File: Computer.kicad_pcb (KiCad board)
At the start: 2 copper layers, 35 parts, among them J1 DB9, J2 Screw_Terminal_1x04, U1 8284, U10 74LS04, U11 7400, U12 8259, U2 LM2931AZ-5.0, U3 8088, U4 74LS04, U5 28C256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

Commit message: Fix GND fill issue
There was an area of the copper fill on B.Cu that wasn't getting any
connection to ground. I fixed this here.
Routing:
- net Net-(U4-Pad10): track 130.2 -> 131.0 mm, vias 2 -> 4
- net Net-(U4-Pad11): track 167.5 -> 168.3 mm, vias 2 -> 4

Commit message: Update to revision A
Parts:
- added R16: 10k, Resistors_THT:R_Axial_DIN0204_L3.6mm_D1.6mm_P7.62mm_Horizontal, F.Cu at (163.8, 57.1)
- added R17: 10k, Resistors_THT:R_Axial_DIN0204_L3.6mm_D1.6mm_P7.62mm_Horizontal, F.Cu at (147.3, 55.9)
- added R4: 10k, Resistors_THT:R_Axial_DIN0204_L3.6mm_D1.6mm_P7.62mm_Horizontal, F.Cu at (139.7, 119.4)
- added R5: 10k, Resistors_THT:R_Axial_DIN0204_L3.6mm_D1.6mm_P7.62mm_Horizontal, F.Cu at (123.2, 134.6)
- added U13: 74LS138, Housings_DIP:DIP-16_W7.62mm, F.Cu at (152.4, 39.4)
- U8: value 7400 -> 74LS138; footprint Housings_DIP:DIP-14_W7.62mm -> Housings_DIP:DIP-16_W7.62mm
- moved R11 60.4 mm to (97.8, 71.1), turned to 90 degrees
- moved C2 57.5 mm to (159.1, 74.9), turned to 0 degrees
- moved U11 47.8 mm to (135.9, 41.9)
- moved U8 47.7 mm to (127.0, 119.4), turned to 0 degrees
- moved R2 47.1 mm to (158.8, 63.5), turned to 270 degrees
- moved R3 45.4 mm to (158.8, 91.4), turned to 270 degrees
- moved BUS1 43.2 mm to (172.7, 123.2)
- moved R1 42.4 mm to (129.5, 48.3), turned to 270 degrees
- moved C4 42.2 mm to (58.4, 109.2)
- moved U5 40.2 mm to (102.9, 63.5)
- moved R8 39.1 mm to (134.6, 78.7), turned to 270 degrees
- moved C1 38.7 mm to (54.6, 48.3), turned to 180 degrees
- moved R10 38.6 mm to (134.6, 90.2), turned to 270 degrees
- moved R12 38.1 mm to (68.6, 113.0)
- moved U7 38.1 mm to (72.4, 63.5)
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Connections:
- U10 pad 10: (no net) -> Net-(U10-Pad10)
- U10 pad 11: (no net) -> WR
- U10 pad 12: (no net) -> Net-(U10-Pad12)
- U10 pad 13: (no net) -> IO/M
- U10 pad 3: IO/M -> RD
- U10 pad 5: IO/M -> RD
- U10 pad 9: IO/M -> RD
- U12 pad 1: Net-(U10-Pad8) -> Net-(U12-Pad1)
- U12 pad 2: Net-(U10-Pad8) -> RD
- U12 pad 3: Net-(U10-Pad8) -> Net-(U10-Pad10)
- U3 pad 32: IO/M -> RD
- U4 pad 10: Net-(U4-Pad10) -> (no net)
- U4 pad 11: Net-(U4-Pad11) -> (no net)
- U4 pad 3: Net-(U4-Pad3) -> (no net)
- U4 pad 4: IO/M -> (no net)
- U4 pad 5: Net-(U4-Pad2) -> (no net)
- U4 pad 6: Net-(U4-Pad3) -> (no net)
- U4 pad 8: Net-(U4-Pad8) -> (no net)
- U4 pad 9: IO/M -> (no net)
- U5 pad 20: Net-(U4-Pad10) -> Net-(U5-Pad20)
- U5 pad 22: IO/M -> RD
- U5 pad 27: Net-(U4-Pad10) -> Net-(R11-Pad1)
- U6 pad 20: Net-(U4-Pad11) -> Net-(U6-Pad20)
- U6 pad 22: IO/M -> RD
- U7 pad 14: Net-(U4-Pad8) -> Net-(U13-Pad15)
- U7 pad 21: IO/M -> Net-(U10-Pad8)
- U8 pad 1: A15 -> A17
- U8 pad 10: Net-(R11-Pad1) -> Net-(U8-Pad10)
- U8 pad 11: (no net) -> Net-(U8-Pad11)
- U8 pad 12: (no net) -> Net-(U8-Pad12)
- U8 pad 13: (no net) -> Net-(U8-Pad13)
- U8 pad 14: Vcc -> Net-(U8-Pad14)
- U8 pad 2: A16 -> A18
- U8 pad 3: Net-(U4-Pad11) -> A19
- U8 pad 4: A17 -> Net-(R5-Pad2)
- U8 pad 5: A18 -> IO/M
- U8 pad 6: Net-(U4-Pad11) -> Net-(R4-Pad2)
- U8 pad 7: GND -> Net-(U5-Pad20)
- U8 pad 8: Net-(U4-Pad11) -> GND
- U8 pad 9: A19 -> Net-(U8-Pad9)
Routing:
- net Net-(U4-Pad11): track 168.3 -> 0.00 mm, vias 4 -> 0
- net RD: track 0.00 -> 159.7 mm, vias 0 -> 3
- net Net-(U4-Pad10): track 131.0 -> 0.00 mm, vias 4 -> 0
- net Net-(U13-Pad15): track 0.00 -> 110.3 mm
- net Net-(U4-Pad8): track 109.5 -> 0.00 mm, vias 1 -> 0
- net IO/M: track 240.1 -> 164.1 mm, vias 3 -> 0
- net WR: track 151.4 -> 219.4 mm, vias 3 -> 0
- net Net-(BUS1-Pad20): track 65.5 -> 131.1 mm, vias 2 -> 3
- net GND: track 589.6 -> 526.7 mm, vias 2 -> 11
- net Net-(BUS1-Pad41): track 110.0 -> 172.9 mm, vias 3 -> 2
- net Net-(BUS1-Pad12): track 112.6 -> 49.9 mm
- net Net-(U10-Pad12): track 0.00 -> 59.8 mm
- net Net-(U5-Pad20): track 0.00 -> 58.0 mm
- net A4: track 282.2 -> 336.1 mm, vias 4 -> 3
- net Net-(U10-Pad10): track 0.00 -> 53.2 mm
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- removed copper zone on B.Cu, net GND
- removed copper zone on F.Cu, net Vcc
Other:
- board text added: "Cut on Line"
- board text added: "Rev. A"
- board text removed: "Cut on line"

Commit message: Add -12v and -5v rails
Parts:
- added U14: LM7905CT, Power_Integrations:TO-220, F.Cu at (52.1, 39.4)
- added U15: LM7912CT, Power_Integrations:TO-220, F.Cu at (64.8, 39.4)
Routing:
- net Net-(BUS1-Pad5): track 0.00 -> 195.4 mm, vias 0 -> 3
- net Net-(BUS1-Pad7): track 0.00 -> 167.9 mm, vias 0 -> 2
- net GND: track 526.7 -> 551.7 mm
- net Net-(J2-Pad4): track 30.0 -> 51.4 mm
- net Net-(J2-Pad1): track 28.8 -> 36.1 mm

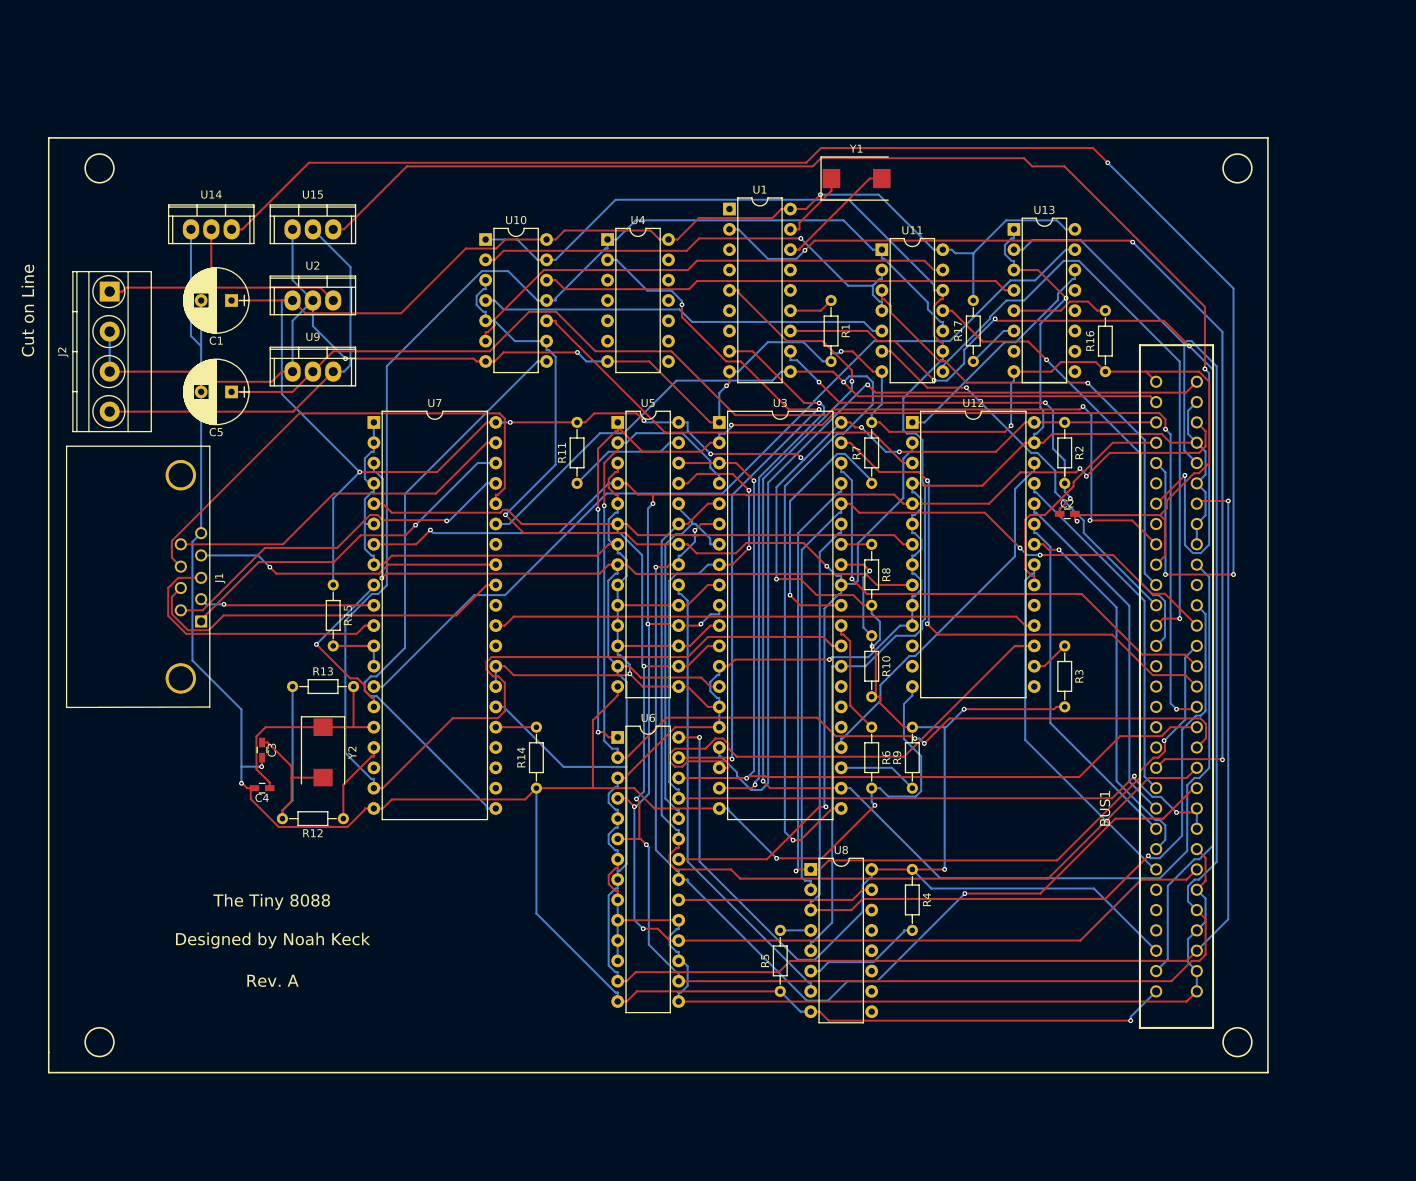
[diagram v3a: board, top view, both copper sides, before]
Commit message: Start adding RS232 level shifters
Signed-off-by: Nkeck720 <noahkeck72@gmail.com>
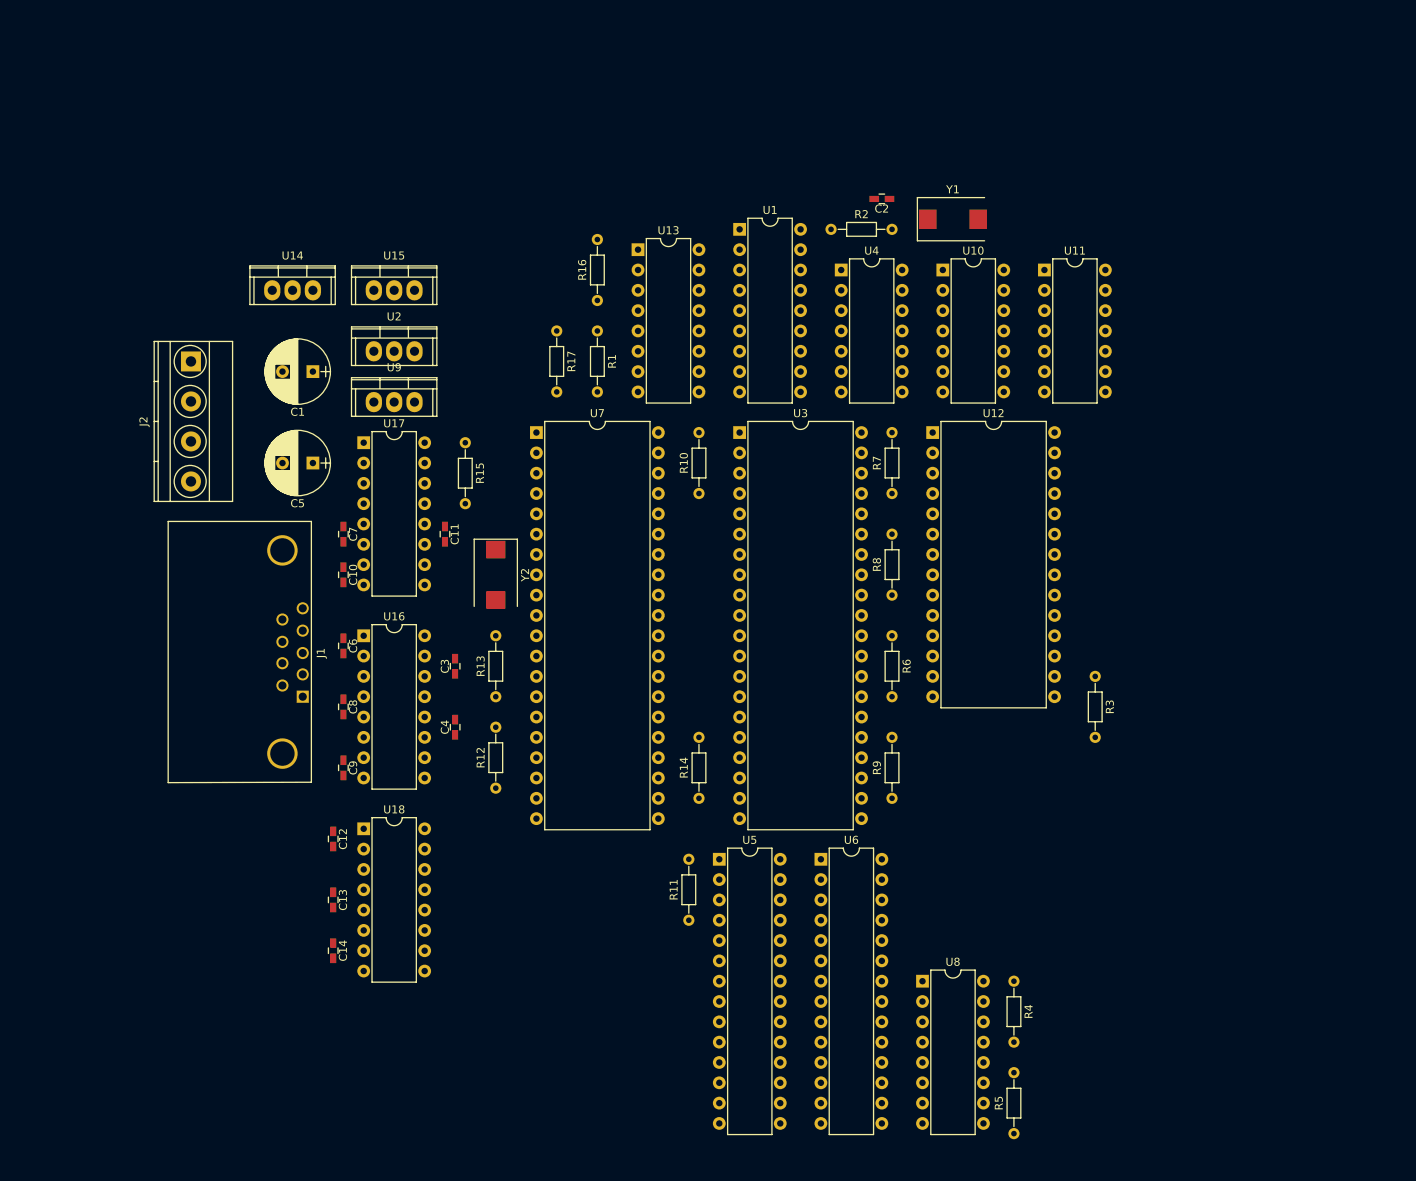
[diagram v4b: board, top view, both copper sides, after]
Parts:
- removed BUS1: BUSPC, Connectors:ISA8
- added C10: 1 uF, Capacitors_SMD:C_0603_HandSoldering, F.Cu at (68.6, 82.5)
- added C11: 1 uF, Capacitors_SMD:C_0603_HandSoldering, F.Cu at (81.3, 77.5)
- added C12: 1 uF, Capacitors_SMD:C_0603_HandSoldering, F.Cu at (67.3, 115.6)
- added C13: 1 uF, Capacitors_SMD:C_0603_HandSoldering, F.Cu at (67.3, 123.2)
- added C14: 1 uF, Capacitors_SMD:C_0603_HandSoldering, F.Cu at (67.3, 129.5)
- added C6: 1 uF, Capacitors_SMD:C_0603_HandSoldering, F.Cu at (68.6, 91.4)
- added C7: 1 uF, Capacitors_SMD:C_0603_HandSoldering, F.Cu at (68.6, 77.5)
- added C8: 1 uF, Capacitors_SMD:C_0603_HandSoldering, F.Cu at (68.6, 99.1)
- added C9: 1 uF, Capacitors_SMD:C_0603_HandSoldering, F.Cu at (68.6, 106.7)
- added U16: MAX202, Housings_DIP:DIP-16_W7.62mm, F.Cu at (71.1, 90.2)
- added U17: MAX202, Housings_DIP:DIP-16_W7.62mm, F.Cu at (71.1, 66.0)
- added U18: MAX202, Housings_DIP:DIP-16_W7.62mm, F.Cu at (71.1, 114.3)
- moved R16 64.1 mm to (100.3, 48.3)
- moved U10 57.3 mm to (143.5, 44.5)
- moved R11 56.4 mm to (111.8, 125.7)
- moved U5 56.1 mm to (115.6, 118.1)
- moved R17 52.2 mm to (95.2, 52.1), turned to 270 degrees
- moved U13 47.1 mm to (105.4, 41.9)
- moved C2 45.7 mm to (135.9, 35.6), turned to 180 degrees
- moved R2 37.9 mm to (129.5, 39.4), turned to 0 degrees
- moved R5 34.2 mm to (152.4, 152.4)
- moved Y2 31.0 mm to (87.6, 82.5)
- moved U6 29.6 mm to (128.3, 118.1)
- moved U4 29.5 mm to (130.8, 44.5)
- moved R1 29.5 mm to (100.3, 52.1)
- moved R10 28.0 mm to (113.0, 72.4), turned to 90 degrees
- moved C3 26.3 mm to (82.5, 94.0), turned to 90 degrees
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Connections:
- U7 pad 10: Net-(J1-Pad2) -> Net-(U16-Pad12)
- U7 pad 11: Net-(J1-Pad3) -> Net-(U16-Pad11)
- U7 pad 32: Net-(J1-Pad7) -> Net-(U17-Pad11)
- U7 pad 33: Net-(J1-Pad4) -> Net-(U16-Pad10)
- U7 pad 36: Net-(J1-Pad8) -> Net-(U17-Pad12)
- U7 pad 37: Net-(J1-Pad6) -> Net-(U16-Pad9)
- U7 pad 38: Net-(J1-Pad1) -> Net-(U17-Pad9)
- U7 pad 39: Net-(J1-Pad9) -> Net-(U18-Pad12)
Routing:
- net GND: track 551.7 -> 0.00 mm, vias 11 -> 0
- net Vcc: track 460.1 -> 0.00 mm, vias 13 -> 0
- net A0: track 443.8 -> 0.00 mm, vias 3 -> 0
- net A4: track 336.1 -> 0.00 mm, vias 3 -> 0
- net A2: track 308.0 -> 0.00 mm, vias 2 -> 0
- net A6: track 258.6 -> 0.00 mm, vias 8 -> 0
- net WR: track 219.4 -> 0.00 mm
- net Net-(BUS1-Pad5): track 195.4 -> 0.00 mm, vias 3 -> 0
- net Net-(BUS1-Pad41): track 172.9 -> 0.00 mm, vias 2 -> 0
- net Net-(BUS1-Pad7): track 167.9 -> 0.00 mm, vias 2 -> 0
- net Net-(BUS1-Pad2): track 166.6 -> 0.00 mm, vias 2 -> 0
- net IO/M: track 164.1 -> 0.00 mm
- net RD: track 159.7 -> 0.00 mm, vias 3 -> 0
- net A14: track 155.0 -> 0.00 mm, vias 5 -> 0
- net Net-(BUS1-Pad30): track 140.7 -> 0.00 mm, vias 3 -> 0
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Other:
- board text removed: "Cut on Line"
- board text removed: "Rev. A"
- board text removed: "The Tiny 8088 Designed by Noah Keck"

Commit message: Finish level shifters
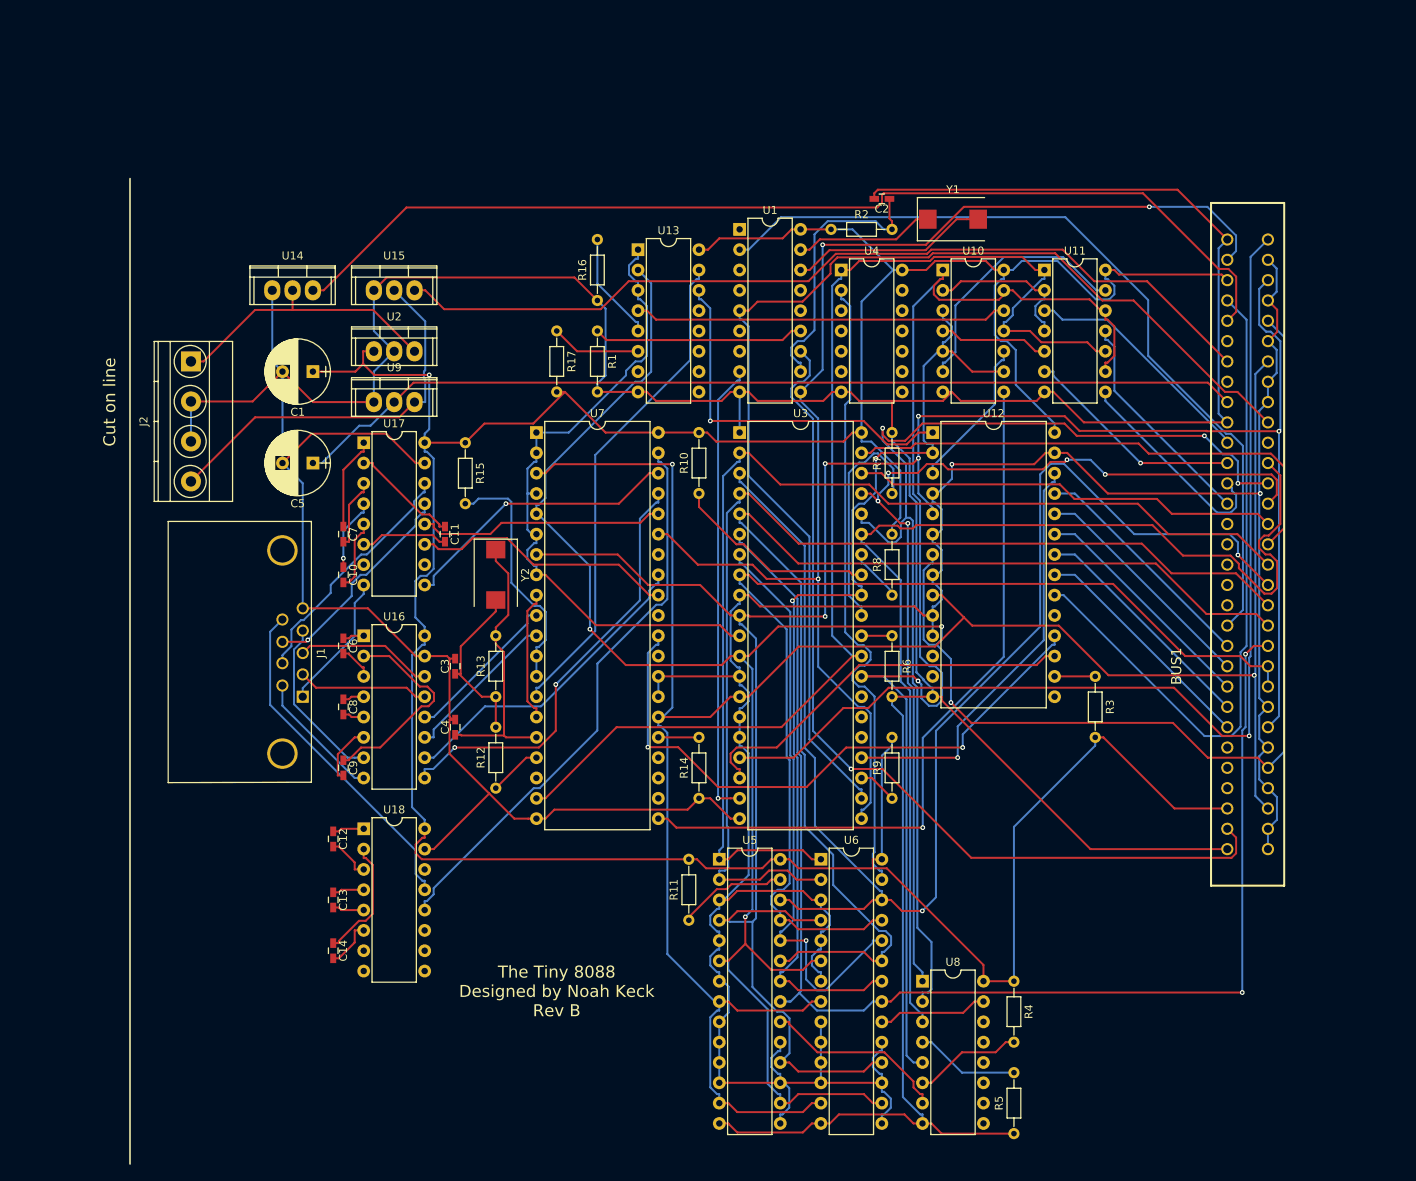
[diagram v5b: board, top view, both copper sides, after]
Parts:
- added BUS1: BUSPC, Connectors:ISA8, F.Cu at (181.6, 105.4)
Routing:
- net GND: track 0.00 -> 583.7 mm
- net Vcc: track 0.00 -> 441.2 mm, vias 0 -> 1
- net A0: track 0.00 -> 421.7 mm, vias 0 -> 2
- net A4: track 0.00 -> 314.9 mm, vias 0 -> 4
- net A6: track 0.00 -> 279.0 mm, vias 0 -> 5
- net A2: track 0.00 -> 276.1 mm, vias 0 -> 2
- net A13: track 0.00 -> 177.1 mm, vias 0 -> 2
- net A10: track 0.00 -> 166.5 mm, vias 0 -> 2
- net IO/M: track 0.00 -> 160.6 mm, vias 0 -> 1
- net Net-(BUS1-Pad2): track 0.00 -> 158.5 mm, vias 0 -> 3
- net A11: track 0.00 -> 150.4 mm
- net WR: track 0.00 -> 149.6 mm
- net Net-(BUS1-Pad41): track 0.00 -> 146.1 mm
- net A19: track 0.00 -> 140.3 mm
- net A18: track 0.00 -> 140.3 mm, vias 0 -> 3
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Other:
- board text added: "Cut on line"
- board text added: "The Tiny 8088 Designed by Noah Keck Rev B"
